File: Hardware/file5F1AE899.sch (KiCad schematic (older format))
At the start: 10 parts, among them U1 SPF5189Z

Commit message: Added discrete Chebyshev input filter to schematic based on Qucs simulationd. Artwork not done. It has occurred to me that I need to do some major cleanup of the test points on this PCBA.
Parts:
- renumbered C11 to C10, C7 to C6, C8 to C7, C9 to C8, C10 to C9
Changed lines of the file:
@@
 $Descr A4 11693 8268
 encoding utf-8
-Sheet 6 12
+Sheet 6 16
 Title ""
 Date ""
@@
 AR Path="/5F19ABE9/5F1BCDB1" Ref="#PWR?"  Part="1"
 AR Path="/5F04F5B6/5F1BCDB1" Ref="#PWR?"  Part="1"
-AR Path="/5F04F5B6/5F1AE89A/5F1BCDB1" Ref="#PWR015"  Part="1"
-F 0 "#PWR015" H 4500 4600 50  0001 C CNN
+AR Path="/5F04F5B6/5F1AE89A/5F1BCDB1" Ref="#PWR012"  Part="1"
+F 0 "#PWR012" H 4500 4600 50  0001 C CNN
 F 1 "GNDA" H 4505 4677 50  0000 C CNN
 F 2 "" H 4500 4850 50  0001 C CNN
@@
 AR Path="/5F19ABE9/5F1BCDB7" Ref="#PWR?"  Part="1"
 AR Path="/5F04F5B6/5F1BCDB7" Ref="#PWR?"  Part="1"
-AR Path="/5F04F5B6/5F1AE89A/5F1BCDB7" Ref="#PWR018"  Part="1"
-F 0 "#PWR018" H 6100 4200 50  0001 C CNN
+AR Path="/5F04F5B6/5F1AE89A/5F1BCDB7" Ref="#PWR015"  Part="1"
+F 0 "#PWR015" H 6100 4200 50  0001 C CNN
 F 1 "GNDA" H 6105 4277 50  0000 C CNN
 F 2 "" H 6100 4450 50  0001 C CNN
@@
 AR Path="/5F19ABE9/5F1BCDC4" Ref="#PWR?"  Part="1"
 AR Path="/5F04F5B6/5F1BCDC4" Ref="#PWR?"  Part="1"
-AR Path="/5F04F5B6/5F1AE89A/5F1BCDC4" Ref="#PWR014"  Part="1"
-F 0 "#PWR014" H 3950 4400 50  0001 C CNN
+AR Path="/5F04F5B6/5F1AE89A/5F1BCDC4" Ref="#PWR011"  Part="1"
+F 0 "#PWR011" H 3950 4400 50  0001 C CNN
 F 1 "GNDA" H 3955 4477 50  0000 C CNN
 F 2 "" H 3950 4650 50  0001 C CNN
@@
 AR Path="/5F19ABE9/5F1BCDDC" Ref="C?"  Part="1"
 AR Path="/5F04F5B6/5F1BCDDC" Ref="C?"  Part="1"
-AR Path="/5F04F5B6/5F1AE89A/5F1BCDDC" Ref="C9"  Part="1"
-F 0 "C9" V 5298 3950 50  0000 C CNN
+AR Path="/5F04F5B6/5F1AE89A/5F1BCDDC" Ref="C8"  Part="1"
+F 0 "C8" V 5298 3950 50  0000 C CNN
 F 1 "600S2R2" V 5389 3950 50  0000 C CNN
 F 2 "Resistor_SMD:R_0603_1608Metric" H 5600 4050 50  0001 C CNN
@@
 AR Path="/5F19ABE9/5F1BCDEE" Ref="C?"  Part="1"
 AR Path="/5F04F5B6/5F1BCDEE" Ref="C?"  Part="1"
-AR Path="/5F04F5B6/5F1AE89A/5F1BCDEE" Ref="C7"  Part="1"
-F 0 "C7" H 4065 4346 50  0000 L CNN
+AR Path="/5F04F5B6/5F1AE89A/5F1BCDEE" Ref="C6"  Part="1"
+F 0 "C6" H 4065 4346 50  0000 L CNN
 F 1 "600S120" H 4065 4255 50  0000 L CNN
 F 2 "Resistor_SMD:R_0603_1608Metric" H 4000 4400 50  0001 C CNN
@@
 AR Path="/5F19ABE9/5F1BCDFD" Ref="C?"  Part="1"
 AR Path="/5F04F5B6/5F1BCDFD" Ref="C?"  Part="1"
-AR Path="/5F04F5B6/5F1AE89A/5F1BCDFD" Ref="C10"  Part="1"
-F 0 "C10" H 6215 2846 50  0000 L CNN
+AR Path="/5F04F5B6/5F1AE89A/5F1BCDFD" Ref="C9"  Part="1"
+F 0 "C9" H 6215 2846 50  0000 L CNN
 F 1 "600S101" H 6215 2755 50  0000 L CNN
 F 2 "Resistor_SMD:R_0603_1608Metric" H 6150 2900 50  0001 C CNN
@@
 AR Path="/5F19ABE9/5F1BCE03" Ref="#PWR?"  Part="1"
 AR Path="/5F04F5B6/5F1BCE03" Ref="#PWR?"  Part="1"
-AR Path="/5F04F5B6/5F1AE89A/5F1BCE03" Ref="#PWR016"  Part="1"
-F 0 "#PWR016" H 5000 2900 50  0001 C CNN
+AR Path="/5F04F5B6/5F1AE89A/5F1BCE03" Ref="#PWR013"  Part="1"
+F 0 "#PWR013" H 5000 2900 50  0001 C CNN
 F 1 "GNDA" H 5005 2977 50  0000 C CNN
 F 2 "" H 5000 3150 50  0001 C CNN
@@
 AR Path="/5F19ABE9/5F1BCE0A" Ref="#PWR?"  Part="1"
 AR Path="/5F04F5B6/5F1BCE0A" Ref="#PWR?"  Part="1"
-AR Path="/5F04F5B6/5F1AE89A/5F1BCE0A" Ref="#PWR017"  Part="1"
-F 0 "#PWR017" H 6100 2900 50  0001 C CNN
+AR Path="/5F04F5B6/5F1AE89A/5F1BCE0A" Ref="#PWR014"  Part="1"
+F 0 "#PWR014" H 6100 2900 50  0001 C CNN
 F 1 "GNDA" H 6105 2977 50  0000 C CNN
 F 2 "" H 6100 3150 50  0001 C CNN
@@
 P 5000 2800
 AR Path="/5F04F5B6/5F1BCE11" Ref="C?"  Part="1"
-AR Path="/5F04F5B6/5F1AE89A/5F1BCE11" Ref="C8"  Part="1"
-F 0 "C8" H 5115 2846 50  0000 L CNN
+AR Path="/5F04F5B6/5F1AE89A/5F1BCE11" Ref="C7"  Part="1"
+F 0 "C7" H 5115 2846 50  0000 L CNN
 F 1 "CC0603KRX7R9BB104" H 5115 2755 50  0000 L CNN
 F 2 "Capacitor_SMD:C_0603_1608Metric" H 5038 2650 50  0001 C CNN
@@
 AR Path="/5F19ABE9/5F283178" Ref="#PWR?"  Part="1"
 AR Path="/5F04F5B6/5F283178" Ref="#PWR?"  Part="1"
-AR Path="/5F04F5B6/5F1AE89A/5F283178" Ref="#PWR019"  Part="1"
-F 0 "#PWR019" H 7800 4700 50  0001 C CNN
+AR Path="/5F04F5B6/5F1AE89A/5F283178" Ref="#PWR016"  Part="1"
+F 0 "#PWR016" H 7800 4700 50  0001 C CNN
 F 1 "GNDA" H 7805 4777 50  0000 C CNN
 F 2 "" H 7800 4950 50  0001 C CNN
@@
 $EndComp
 $Comp
-L ATC:600S101_3-pad-R C11
+L ATC:600S101_3-pad-R C10
 U 1 1 5F3AD87D
 P 7400 3950
-F 0 "C11" H 7400 4202 50  0000 C CNN
+F 0 "C10" H 7400 4202 50  0000 C CNN
 F 1 "600S101_3-pad-R" H 7400 4111 50  0000 C CNN
 F 2 "Capacitor_SMD:C_0603_1608Metric_3-pad-R" H 8300 3200 50  0001 C CNN

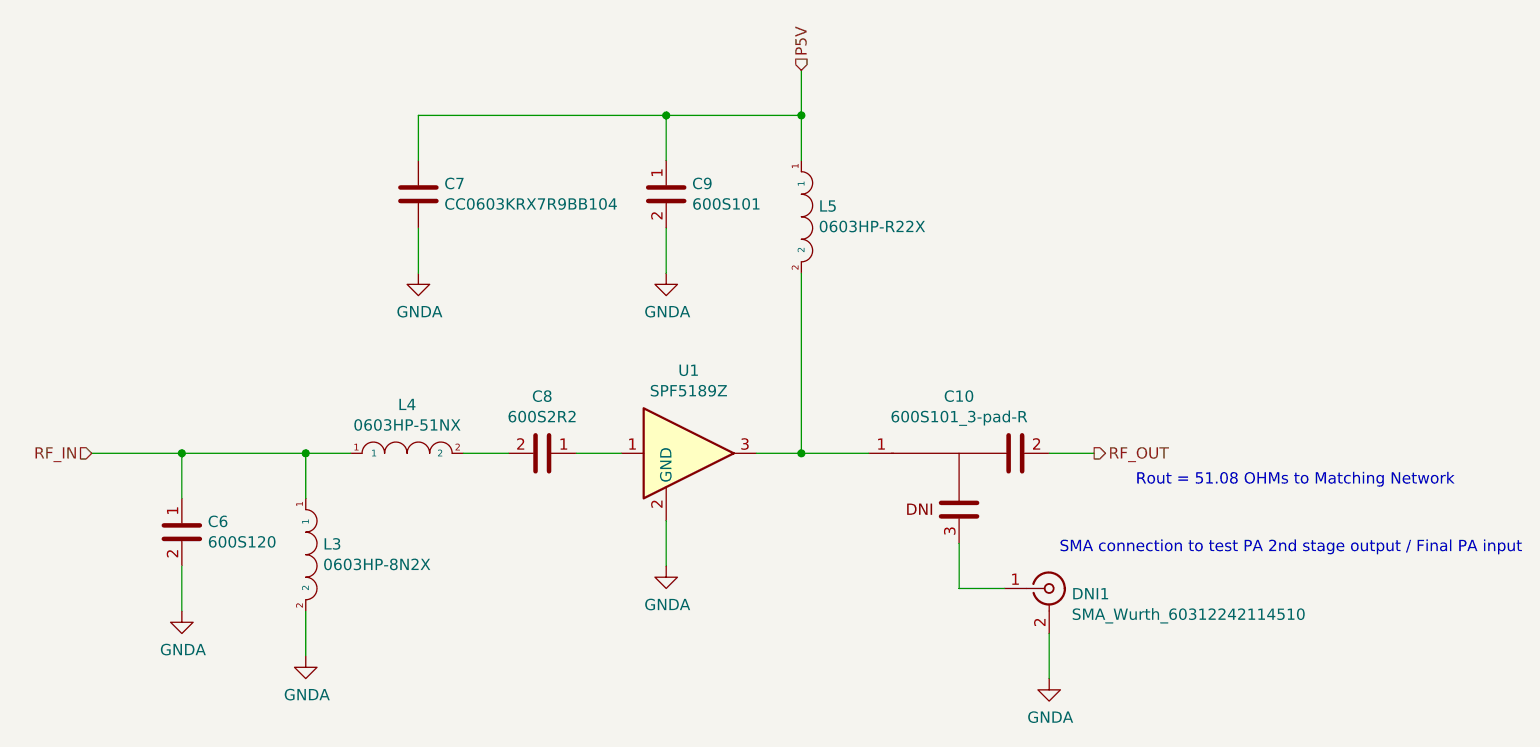
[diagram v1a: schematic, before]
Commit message: Major cleanup to both the schematic and directory structure. Stackup has changed accomodate to 0.65mm trace width. Chebyshev filter lived through the experience in the Qucs simulation; others not checked yet. I do want to re-visit the matching networks of all of the amplifiers as I have developed some good strategies to implement them.
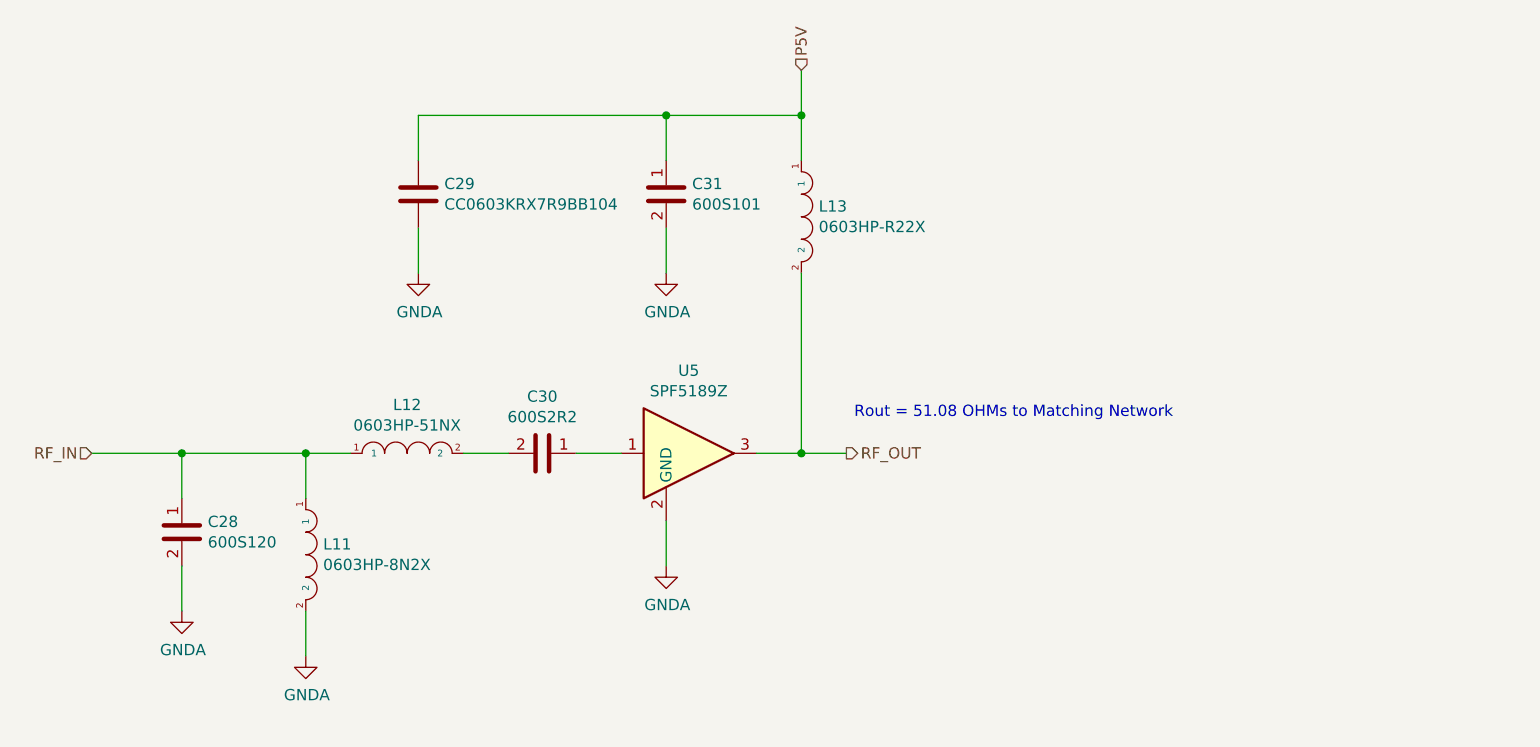
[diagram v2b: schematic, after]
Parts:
- removed C10: 600S101_3-pad-R, Capacitor_SMD:C_0603_1608Metric_3-pad-R, symbol ATC:600S101_3-pad-R
- removed DNI1: SMA_Wurth_60312242114510, RF:SMA_Wurth_60312242114510, symbol RF:SMA_Wurth_60312242114510
- renumbered C6 to C28, C7 to C29, C8 to C30, C9 to C31, L3 to L11, L4 to L12, L5 to L13, U1 to U5
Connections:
- net RF_OUT: now also L13.2, U5.3
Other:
- note removed: "SMA connection to test PA 2nd stage output / Final PA input"
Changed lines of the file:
@@
 $Descr A4 11693 8268
 encoding utf-8
-Sheet 6 16
+Sheet 17 24
 Title ""
 Date ""
@@
 AR Path="/5F19ABE9/5F1BCDB1" Ref="#PWR?"  Part="1"
 AR Path="/5F04F5B6/5F1BCDB1" Ref="#PWR?"  Part="1"
-AR Path="/5F04F5B6/5F1AE89A/5F1BCDB1" Ref="#PWR012"  Part="1"
-F 0 "#PWR012" H 4500 4600 50  0001 C CNN
+AR Path="/5F04F5B6/5F1AE89A/5F1BCDB1" Ref="#PWR?"  Part="1"
+AR Path="/5F204DEC/5F205D8E/5F1AE89A/5F1BCDB1" Ref="#PWR035"  Part="1"
+F 0 "#PWR035" H 4500 4600 50  0001 C CNN
 F 1 "GNDA" H 4505 4677 50  0000 C CNN
 F 2 "" H 4500 4850 50  0001 C CNN
@@
 AR Path="/5F19ABE9/5F1BCDB7" Ref="#PWR?"  Part="1"
 AR Path="/5F04F5B6/5F1BCDB7" Ref="#PWR?"  Part="1"
-AR Path="/5F04F5B6/5F1AE89A/5F1BCDB7" Ref="#PWR015"  Part="1"
-F 0 "#PWR015" H 6100 4200 50  0001 C CNN
+AR Path="/5F04F5B6/5F1AE89A/5F1BCDB7" Ref="#PWR?"  Part="1"
+AR Path="/5F204DEC/5F205D8E/5F1AE89A/5F1BCDB7" Ref="#PWR038"  Part="1"
+F 0 "#PWR038" H 6100 4200 50  0001 C CNN
 F 1 "GNDA" H 6105 4277 50  0000 C CNN
 F 2 "" H 6100 4450 50  0001 C CNN
@@
 AR Path="/5F19ABE9/5F1BCDC4" Ref="#PWR?"  Part="1"
 AR Path="/5F04F5B6/5F1BCDC4" Ref="#PWR?"  Part="1"
-AR Path="/5F04F5B6/5F1AE89A/5F1BCDC4" Ref="#PWR011"  Part="1"
-F 0 "#PWR011" H 3950 4400 50  0001 C CNN
+AR Path="/5F04F5B6/5F1AE89A/5F1BCDC4" Ref="#PWR?"  Part="1"
+AR Path="/5F204DEC/5F205D8E/5F1AE89A/5F1BCDC4" Ref="#PWR034"  Part="1"
+F 0 "#PWR034" H 3950 4400 50  0001 C CNN
 F 1 "GNDA" H 3955 4477 50  0000 C CNN
 F 2 "" H 3950 4650 50  0001 C CNN
@@
 AR Path="/5F19ABE9/5F1BCDCB" Ref="L?"  Part="1"
 AR Path="/5F04F5B6/5F1BCDCB" Ref="L?"  Part="1"
-AR Path="/5F04F5B6/5F1AE89A/5F1BCDCB" Ref="L5"  Part="1"
-F 0 "L5" V 6654 2977 50  0000 L CNN
+AR Path="/5F04F5B6/5F1AE89A/5F1BCDCB" Ref="L?"  Part="1"
+AR Path="/5F204DEC/5F205D8E/5F1AE89A/5F1BCDCB" Ref="L13"  Part="1"
+F 0 "L13" V 6654 2977 50  0000 L CNN
 F 1 "0603HP-R22X" V 6745 2977 50  0000 L CNN
 F 2 "Resistor_SMD:R_0603_1608Metric" H 6450 3050 50  0001 C CNN
@@
 AR Path="/5F19ABE9/5F1BCDDC" Ref="C?"  Part="1"
 AR Path="/5F04F5B6/5F1BCDDC" Ref="C?"  Part="1"
-AR Path="/5F04F5B6/5F1AE89A/5F1BCDDC" Ref="C8"  Part="1"
-F 0 "C8" V 5298 3950 50  0000 C CNN
+AR Path="/5F04F5B6/5F1AE89A/5F1BCDDC" Ref="C?"  Part="1"
+AR Path="/5F204DEC/5F205D8E/5F1AE89A/5F1BCDDC" Ref="C30"  Part="1"
+F 0 "C30" V 5298 3950 50  0000 C CNN
 F 1 "600S2R2" V 5389 3950 50  0000 C CNN
 F 2 "Resistor_SMD:R_0603_1608Metric" H 5600 4050 50  0001 C CNN
@@
 AR Path="/5F19ABE9/5F1BCDE2" Ref="L?"  Part="1"
 AR Path="/5F04F5B6/5F1BCDE2" Ref="L?"  Part="1"
-AR Path="/5F04F5B6/5F1AE89A/5F1BCDE2" Ref="L4"  Part="1"
-F 0 "L4" H 4950 4165 50  0000 C CNN
+AR Path="/5F04F5B6/5F1AE89A/5F1BCDE2" Ref="L?"  Part="1"
+AR Path="/5F204DEC/5F205D8E/5F1AE89A/5F1BCDE2" Ref="L12"  Part="1"
+F 0 "L12" H 4950 4165 50  0000 C CNN
 F 1 "0603HP-51NX" H 4950 4074 50  0000 C CNN
 F 2 "Resistor_SMD:R_0603_1608Metric" H 4700 4100 50  0001 C CNN
@@
 AR Path="/5F19ABE9/5F1BCDE8" Ref="L?"  Part="1"
 AR Path="/5F04F5B6/5F1BCDE8" Ref="L?"  Part="1"
-AR Path="/5F04F5B6/5F1AE89A/5F1BCDE8" Ref="L3"  Part="1"
-F 0 "L3" V 4454 4477 50  0000 L CNN
+AR Path="/5F04F5B6/5F1AE89A/5F1BCDE8" Ref="L?"  Part="1"
+AR Path="/5F204DEC/5F205D8E/5F1AE89A/5F1BCDE8" Ref="L11"  Part="1"
+F 0 "L11" V 4454 4477 50  0000 L CNN
 F 1 "0603HP-8N2X" V 4545 4477 50  0000 L CNN
 F 2 "Resistor_SMD:R_0603_1608Metric" H 4250 4550 50  0001 C CNN
@@
 AR Path="/5F19ABE9/5F1BCDEE" Ref="C?"  Part="1"
 AR Path="/5F04F5B6/5F1BCDEE" Ref="C?"  Part="1"
-AR Path="/5F04F5B6/5F1AE89A/5F1BCDEE" Ref="C6"  Part="1"
-F 0 "C6" H 4065 4346 50  0000 L CNN
+AR Path="/5F04F5B6/5F1AE89A/5F1BCDEE" Ref="C?"  Part="1"
+AR Path="/5F204DEC/5F205D8E/5F1AE89A/5F1BCDEE" Ref="C28"  Part="1"
+F 0 "C28" H 4065 4346 50  0000 L CNN
 F 1 "600S120" H 4065 4255 50  0000 L CNN
 F 2 "Resistor_SMD:R_0603_1608Metric" H 4000 4400 50  0001 C CNN
@@
 AR Path="/5F19ABE9/5F1BCDFD" Ref="C?"  Part="1"
 AR Path="/5F04F5B6/5F1BCDFD" Ref="C?"  Part="1"
-AR Path="/5F04F5B6/5F1AE89A/5F1BCDFD" Ref="C9"  Part="1"
-F 0 "C9" H 6215 2846 50  0000 L CNN
+AR Path="/5F04F5B6/5F1AE89A/5F1BCDFD" Ref="C?"  Part="1"
+AR Path="/5F204DEC/5F205D8E/5F1AE89A/5F1BCDFD" Ref="C31"  Part="1"
+F 0 "C31" H 6215 2846 50  0000 L CNN
 F 1 "600S101" H 6215 2755 50  0000 L CNN
 F 2 "Resistor_SMD:R_0603_1608Metric" H 6150 2900 50  0001 C CNN
@@
 AR Path="/5F19ABE9/5F1BCE03" Ref="#PWR?"  Part="1"
 AR Path="/5F04F5B6/5F1BCE03" Ref="#PWR?"  Part="1"
-AR Path="/5F04F5B6/5F1AE89A/5F1BCE03" Ref="#PWR013"  Part="1"
-F 0 "#PWR013" H 5000 2900 50  0001 C CNN
+AR Path="/5F04F5B6/5F1AE89A/5F1BCE03" Ref="#PWR?"  Part="1"
+AR Path="/5F204DEC/5F205D8E/5F1AE89A/5F1BCE03" Ref="#PWR036"  Part="1"
+F 0 "#PWR036" H 5000 2900 50  0001 C CNN
 F 1 "GNDA" H 5005 2977 50  0000 C CNN
 F 2 "" H 5000 3150 50  0001 C CNN
@@
 AR Path="/5F19ABE9/5F1BCE0A" Ref="#PWR?"  Part="1"
 AR Path="/5F04F5B6/5F1BCE0A" Ref="#PWR?"  Part="1"
-AR Path="/5F04F5B6/5F1AE89A/5F1BCE0A" Ref="#PWR014"  Part="1"
-F 0 "#PWR014" H 6100 2900 50  0001 C CNN
+AR Path="/5F04F5B6/5F1AE89A/5F1BCE0A" Ref="#PWR?"  Part="1"
+AR Path="/5F204DEC/5F205D8E/5F1AE89A/5F1BCE0A" Ref="#PWR037"  Part="1"
+F 0 "#PWR037" H 6100 2900 50  0001 C CNN
 F 1 "GNDA" H 6105 2977 50  0000 C CNN
 F 2 "" H 6100 3150 50  0001 C CNN
@@
 P 5000 2800
 AR Path="/5F04F5B6/5F1BCE11" Ref="C?"  Part="1"
-AR Path="/5F04F5B6/5F1AE89A/5F1BCE11" Ref="C7"  Part="1"
-F 0 "C7" H 5115 2846 50  0000 L CNN
+AR Path="/5F04F5B6/5F1AE89A/5F1BCE11" Ref="C?"  Part="1"
+AR Path="/5F204DEC/5F205D8E/5F1AE89A/5F1BCE11" Ref="C29"  Part="1"
+F 0 "C29" H 5115 2846 50  0000 L CNN
 F 1 "CC0603KRX7R9BB104" H 5115 2755 50  0000 L CNN
 F 2 "Capacitor_SMD:C_0603_1608Metric" H 5038 2650 50  0001 C CNN
@@
 	5000 2450 6100 2450
 Connection ~ 6100 2450
-Connection ~ 6700 3950
-Wire Wire Line
-	6700 3950 7000 3950
-Text HLabel 8000 3950 2    50   Output ~ 0
+Text HLabel 6900 3950 2    50   Output ~ 0
 RF_OUT
 Wire Wire Line
-	7800 3950 8000 3950
-Text Notes 9600 4100 2    50   ~ 0
+	6700 3950 6900 3950
+Text Notes 8350 3800 2    50   ~ 0
 Rout = 51.08 OHMs to Matching Network
-$Comp
-L RF:SMA_Wurth_60312242114510 DNI1
-U 1 1 5F27FE71
-P 7800 4550
-F 0 "DNI1" H 7900 4525 50  0000 L CNN
-F 1 "SMA_Wurth_60312242114510" H 7900 4434 50  0000 L CNN
-F 2 "RF:SMA_Wurth_60312242114510" H 7800 4550 50  0001 C CNN
-F 3 "https://www.we-online.de/katalog/datasheet/60312242114510.pdf" H 7800 4550 50  0001 C CNN
-	1    7800 4550
-	1    0    0    -1
-$EndComp
-$Comp
-L power:GNDA #PWR?
-U 1 1 5F283178
-P 7800 4950
-AR Path="/503BB638/5F283178" Ref="#PWR?"  Part="1"
-AR Path="/5F1E02B6/5F283178" Ref="#PWR?"  Part="1"
-AR Path="/5F042EDC/5F283178" Ref="#PWR?"  Part="1"
-AR Path="/5F19ABE9/5F283178" Ref="#PWR?"  Part="1"
-AR Path="/5F04F5B6/5F283178" Ref="#PWR?"  Part="1"
-AR Path="/5F04F5B6/5F1AE89A/5F283178" Ref="#PWR016"  Part="1"
-F 0 "#PWR016" H 7800 4700 50  0001 C CNN
-F 1 "GNDA" H 7805 4777 50  0000 C CNN
-F 2 "" H 7800 4950 50  0001 C CNN
-F 3 "" H 7800 4950 50  0001 C CNN
-	1    7800 4950
-	1    0    0    -1
-$EndComp
-Wire Wire Line
-	7800 4750 7800 4950
-Wire Wire Line
-	7400 4350 7400 4550
-Wire Wire Line
-	7400 4550 7600 4550
-Text Notes 9900 4400 2    50   ~ 0
-SMA connection to test PA 2nd stage output / Final PA input
 $Comp
 L RF_Amplifier:SPF5189Z U?
@@
 AR Path="/5F19ABE9/5F1BCDBE" Ref="U?"  Part="1"
 AR Path="/5F04F5B6/5F1BCDBE" Ref="U?"  Part="1"
-AR Path="/5F04F5B6/5F1AE89A/5F1BCDBE" Ref="U1"  Part="1"
-F 0 "U1" H 6200 4317 50  0000 C CNN
+AR Path="/5F04F5B6/5F1AE89A/5F1BCDBE" Ref="U?"  Part="1"
+AR Path="/5F204DEC/5F205D8E/5F1AE89A/5F1BCDBE" Ref="U5"  Part="1"
+F 0 "U5" H 6200 4317 50  0000 C CNN
 F 1 "SPF5189Z" H 6200 4226 50  0000 C CNN
 F 2 "RF:SOT-89-3_Qorvo_SPF5189z" H 6250 4350 50  0001 C CNN
@@
 	1    0    0    -1
 $EndComp
-$Comp
-L ATC:600S101_3-pad-R C10
-U 1 1 5F3AD87D
-P 7400 3950
-F 0 "C10" H 7400 4202 50  0000 C CNN
-F 1 "600S101_3-pad-R" H 7400 4111 50  0000 C CNN
-F 2 "Capacitor_SMD:C_0603_1608Metric_3-pad-R" H 8300 3200 50  0001 C CNN
-F 3 "" V 7400 3900 50  0001 C CNN
-	1    7400 3950
-	-1   0    0    -1
-$EndComp
+Connection ~ 6700 3950
 $EndSCHEMATC
